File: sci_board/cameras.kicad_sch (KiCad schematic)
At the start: 4 parts, among them X1 TG2520SMN 24.0000M-MCGNNM0

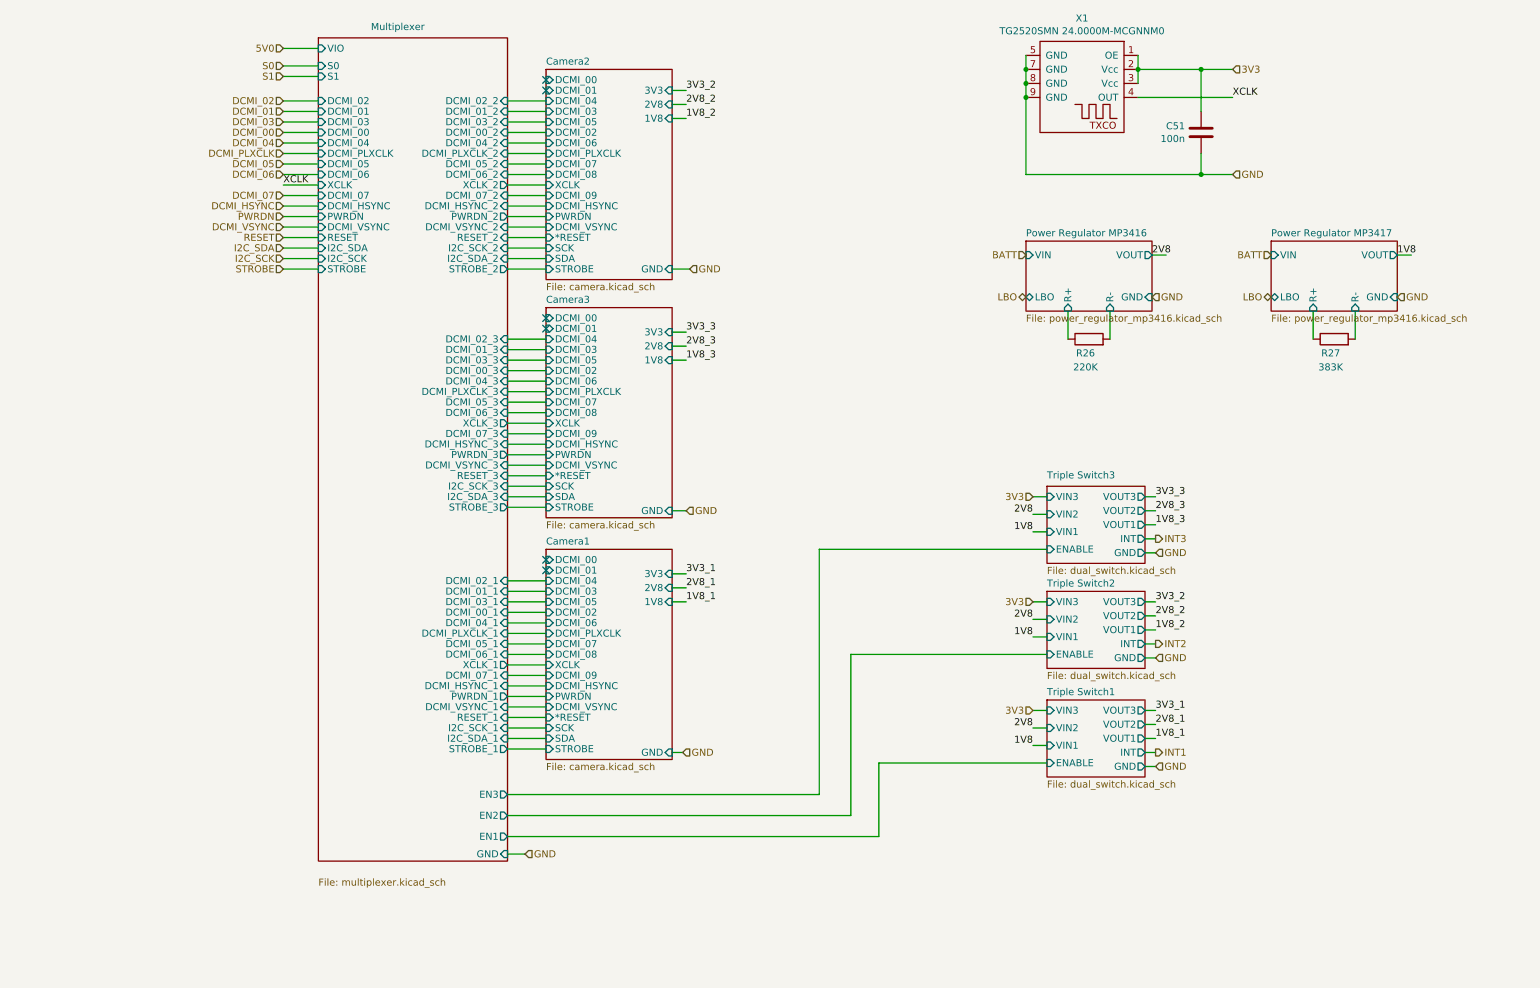
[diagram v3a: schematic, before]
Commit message: replace big multiplexers with tiny ones, replace boost converters with true ones
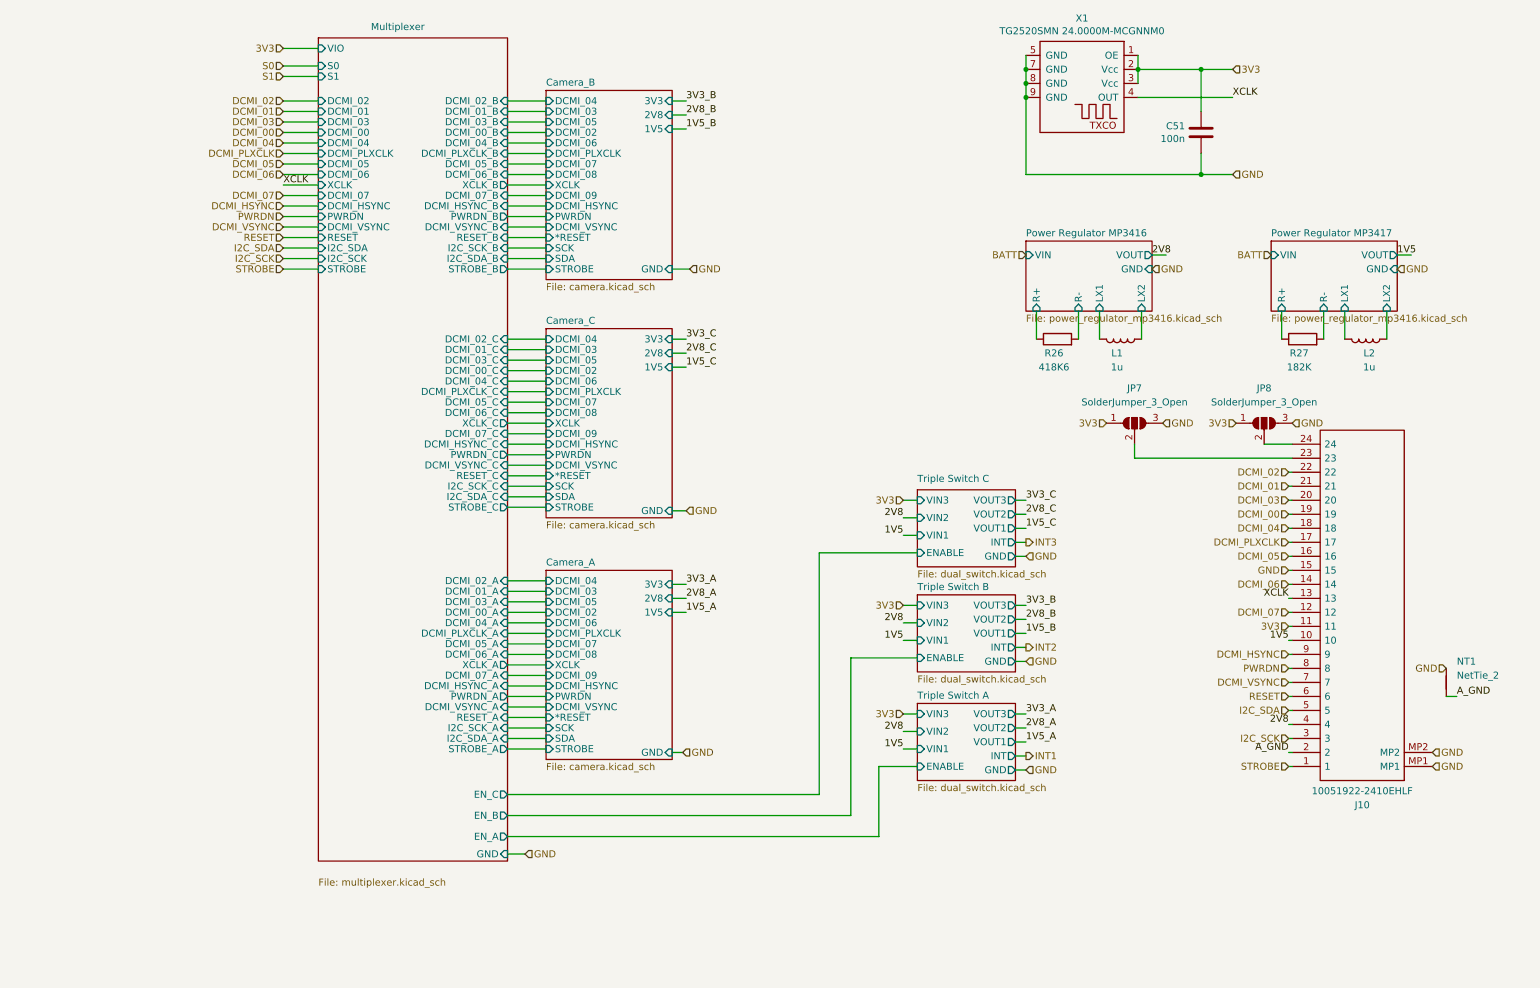
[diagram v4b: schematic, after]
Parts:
- added J10: 10051922-2410EHLF, Project:100519222410EHLF, symbol Project:10051922-2410EHLF
- added JP7, JP8: SolderJumper_3_Open, Jumper:SolderJumper-3_P2.0mm_Open_TrianglePad1.0x1.5mm, symbol Jumper:SolderJumper_3_Open
- added L1, L2: 1u, Inductor_SMD:L_1008_2520Metric_Pad1.43x2.20mm_HandSolder, symbol Device:L
- added NT1: NetTie_2, Project:NetTie-2_SMD_Pad0.3mm, symbol Device:NetTie_2
- R26: value 220K -> 418K6
- R27: value 383K -> 182K
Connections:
- net 2V8: now also J10.4
- net 3V3: now also J10.11, JP7.1 (A), JP8.1 (A)
- net DCMI_00: now also J10.19
- net DCMI_01: now also J10.21
- net DCMI_02: now also J10.22
- net DCMI_03: now also J10.20
- net DCMI_04: now also J10.18
- net DCMI_05: now also J10.16
- net DCMI_06: now also J10.14
- net DCMI_07: now also J10.12
- net DCMI_HSYNC: now also J10.9
- net DCMI_PLXCLK: now also J10.17
- net DCMI_VSYNC: now also J10.7
- net GND: now also J10.15, J10.MP1, J10.MP2, JP7.3 (B), JP8.3 (B), NT1.2
- net I2C_SCK: now also J10.3
- net I2C_SDA: now also J10.5
- net PWRDN: now also J10.8
- net RESET: now also J10.6
- net STROBE: now also J10.1
- net XCLK: now also J10.13
- new net: J10.24, JP8.2 (C)
- new net: J10.23, JP7.2 (C)
- new net 1V5: J10.10
- new net A_GND: J10.2, NT1.1
- new net Power Regulator MP3416/LX1: L1.2
- new net Power Regulator MP3416/LX2: L1.1
- new net Power Regulator MP3417/LX1: L2.2
- new net Power Regulator MP3417/LX2: L2.1
- no-connect marks 6 -> 0
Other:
- sheet Camera1 renamed Camera_A
- sheet Camera2 renamed Camera_B
- sheet Camera3 renamed Camera_C
- sheet Triple Switch1 renamed Triple Switch A
- sheet Triple Switch2 renamed Triple Switch B
- sheet Triple Switch3 renamed Triple Switch C
- sheet Camera_A ports: added 1V5; removed 1V8, DCMI_00, DCMI_01
- sheet Camera_B ports: added 1V5; removed 1V8, DCMI_00, DCMI_01
- sheet Camera_C ports: added 1V5; removed 1V8, DCMI_00, DCMI_01
- sheet Multiplexer ports: added DCMI_00_A, DCMI_00_B, DCMI_00_C, DCMI_01_A, DCMI_01_B, DCMI_01_C, DCMI_02_A, DCMI_02_B, DCMI_02_C, DCMI_03_A, DCMI_03_B, DCMI_03_C, DCMI_04_A, DCMI_04_B, DCMI_04_C, DCMI_05_A, DCMI_05_B, DCMI_05_C, DCMI_06_A, DCMI_06_B, DCMI_06_C, DCMI_07_A, DCMI_07_B, DCMI_07_C, DCMI_HSYNC_A, DCMI_HSYNC_B, DCMI_HSYNC_C, DCMI_PLXCLK_A, DCMI_PLXCLK_B, DCMI_PLXCLK_C, DCMI_VSYNC_A, DCMI_VSYNC_B, DCMI_VSYNC_C, EN_A, EN_B, EN_C, I2C_SCK_A, I2C_SCK_B, I2C_SCK_C, I2C_SDA_A, I2C_SDA_B, I2C_SDA_C, PWRDN_A, PWRDN_B, PWRDN_C, RESET_A, RESET_B, RESET_C, STROBE_A, STROBE_B, STROBE_C, XCLK_A, XCLK_B, XCLK_C; removed DCMI_00_1, DCMI_00_2, DCMI_00_3, DCMI_01_1, DCMI_01_2, DCMI_01_3, DCMI_02_1, DCMI_02_2, DCMI_02_3, DCMI_03_1, DCMI_03_2, DCMI_03_3, DCMI_04_1, DCMI_04_2, DCMI_04_3, DCMI_05_1, DCMI_05_2, DCMI_05_3, DCMI_06_1, DCMI_06_2, DCMI_06_3, DCMI_07_1, DCMI_07_2, DCMI_07_3, DCMI_HSYNC_1, DCMI_HSYNC_2, DCMI_HSYNC_3, DCMI_PLXCLK_1, DCMI_PLXCLK_2, DCMI_PLXCLK_3, DCMI_VSYNC_1, DCMI_VSYNC_2, DCMI_VSYNC_3, EN1, EN2, EN3, I2C_SCK_1, I2C_SCK_2, I2C_SCK_3, I2C_SDA_1, I2C_SDA_2, I2C_SDA_3, PWRDN_1, PWRDN_2, PWRDN_3, RESET_1, RESET_2, RESET_3, STROBE_1, STROBE_2, STROBE_3, XCLK_1, XCLK_2, XCLK_3
- sheet Power Regulator MP3416 ports: added LX1, LX2; removed LBO
- sheet Power Regulator MP3417 ports: added LX1, LX2; removed LBO
- moved on the sheet: R26, R27

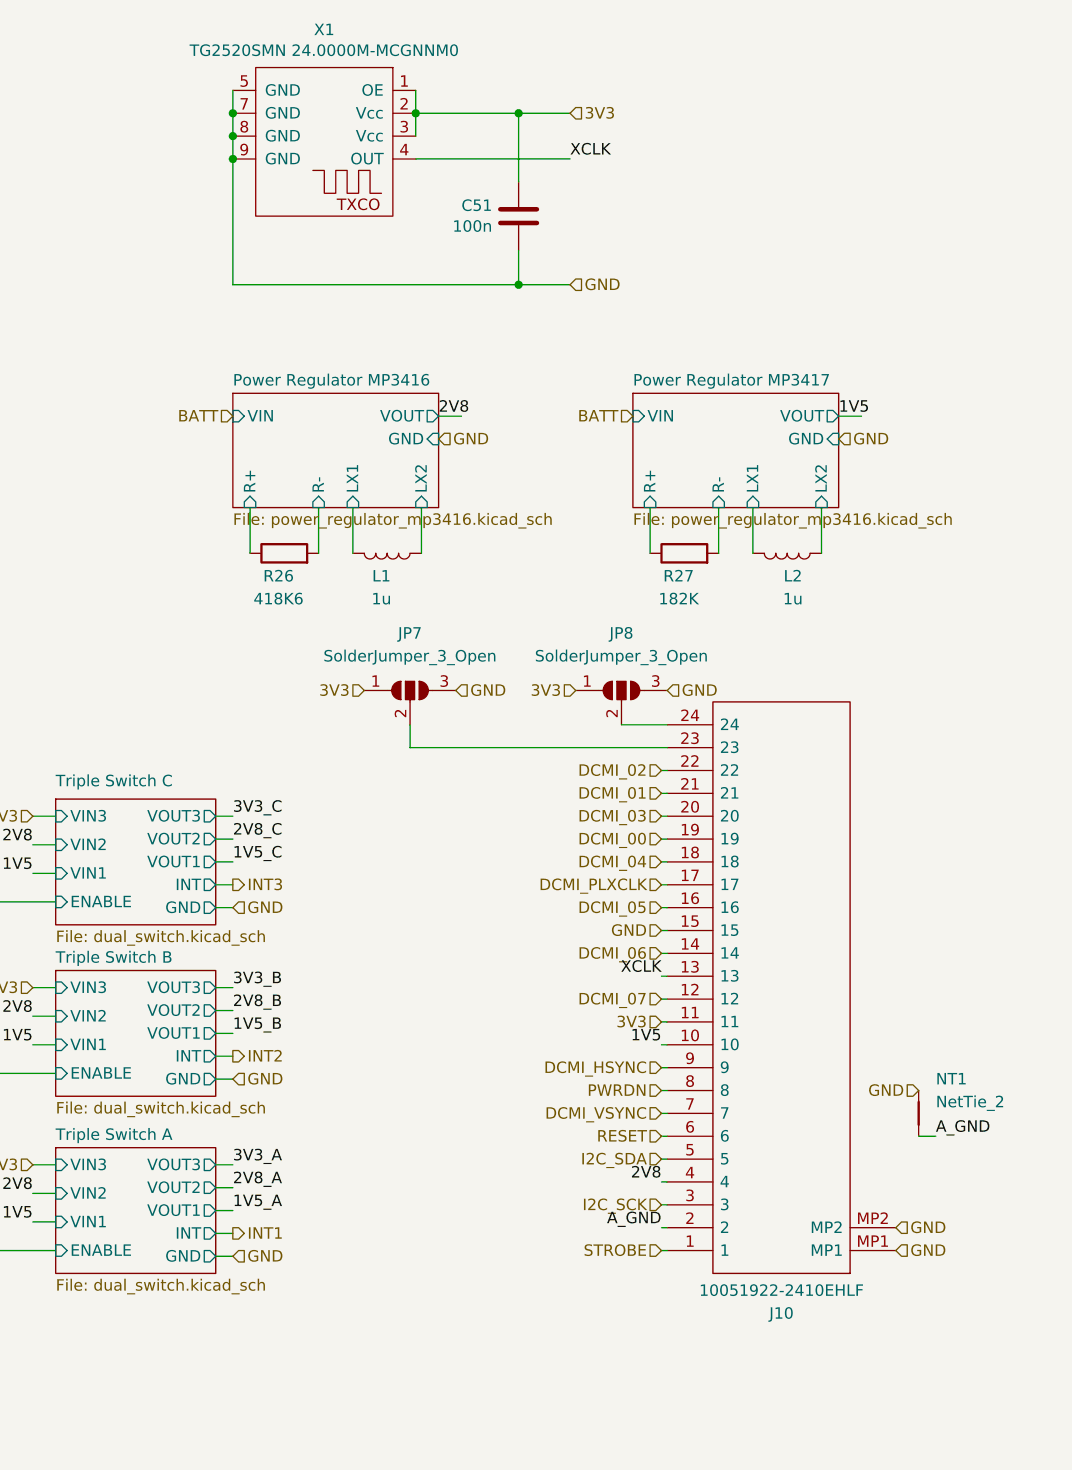
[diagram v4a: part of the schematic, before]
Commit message: changed over SCI to smaller footprint switches
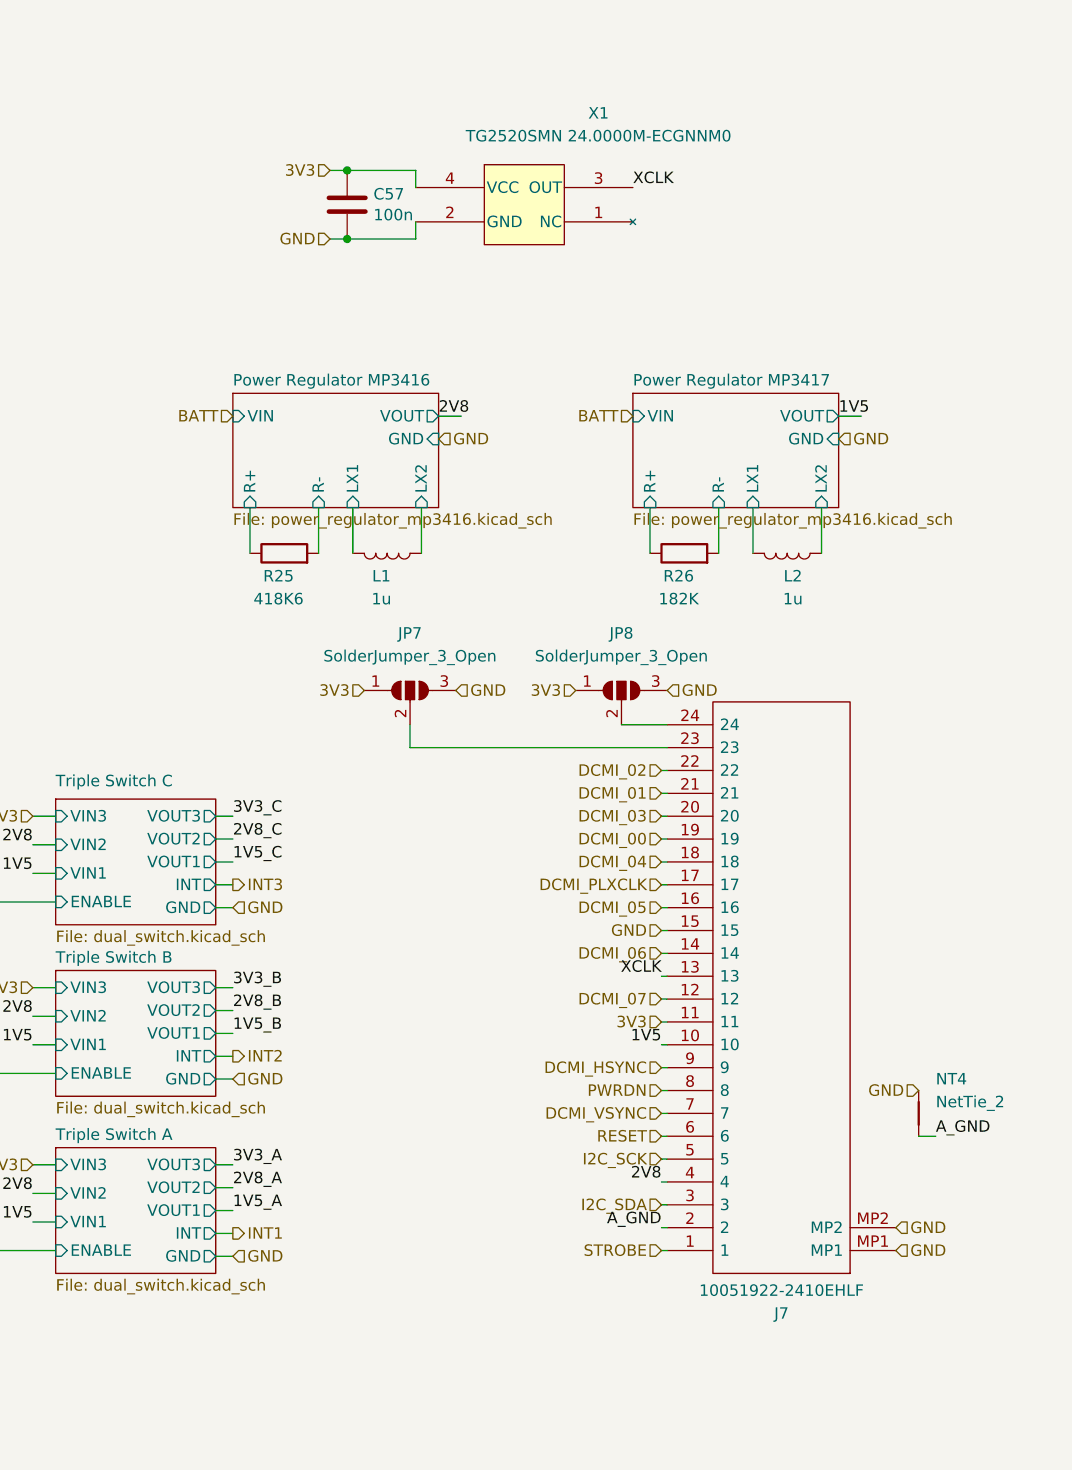
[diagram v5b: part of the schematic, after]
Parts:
- removed C51: 100n, Capacitor_SMD:C_0402_1005Metric_Pad0.74x0.62mm_HandSolder, symbol Device:C
- removed X1: TG2520SMN 24.0000M-MCGNNM0, Project:TG-3541CE_EPS, symbol Project:TG-3541CE-1K
- added C57: 100n, Capacitor_SMD:C_0402_1005Metric_Pad0.74x0.62mm_HandSolder, symbol Device:C
- added X1: TG2520SMN 24.0000M-ECGNNM0, Project:TG2520_EPS, symbol Project:TG2520SMN_EPS
- renumbered J10 to J7, NT1 to NT4, R26 to R25, R27 to R26
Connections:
- net 3V3: now also C57.1, X1.4 (VCC)
- net GND: now also C57.2, X1.2 (GND)
- net I2C_SCK: now also J7.5; no longer J7.3
- net I2C_SDA: now also J7.3; no longer J7.5
- net XCLK: now also X1.3 (OUT)

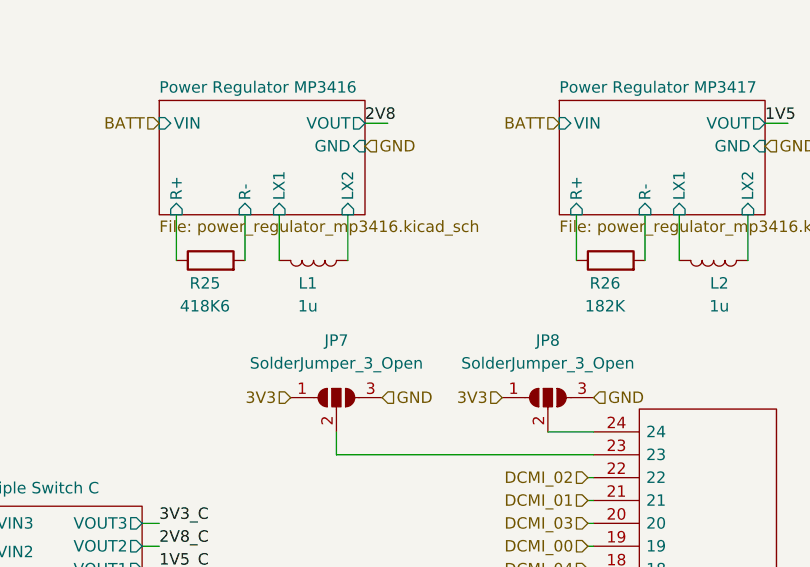
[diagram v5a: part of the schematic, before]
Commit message: replace nearly all buck converters with boost buck (missing is 5raw
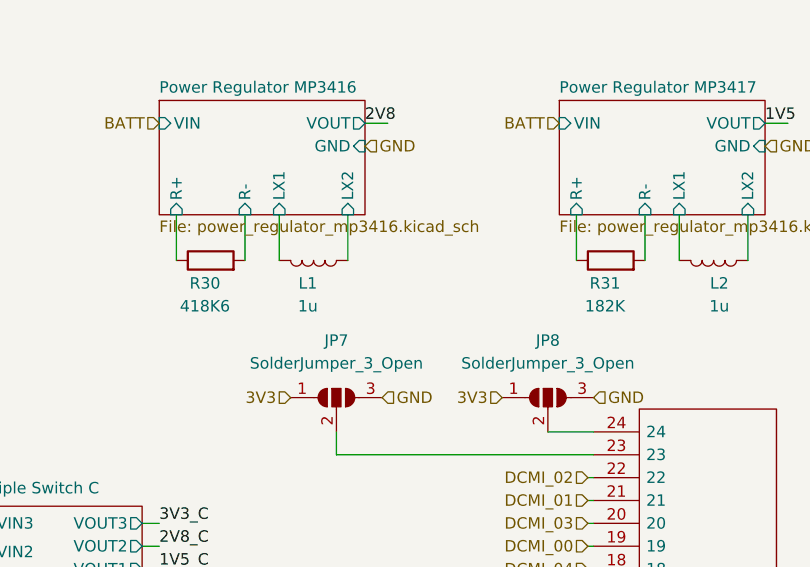
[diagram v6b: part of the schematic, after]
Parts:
- renumbered R25 to R30, R26 to R31
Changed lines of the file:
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@@
 		(on_board yes)
 		(dnp no)
-		(property "Reference" "R25"
+		(property "Reference" "R30"
 			(at 201.93 81.28 90)
 			(effects
@@
 			(project "sci_board"
 				(path "/b4b2c88d-f6cd-4e60-862d-e21f68728580/5e5b27f8-7a4c-45d0-95f8-aff71797fcd3"
-					(reference "R25")
+					(reference "R30")
 					(unit 1)
 				)
@@
 		(on_board yes)
 		(dnp no)
-		(property "Reference" "R26"
+		(property "Reference" "R31"
 			(at 246.38 81.28 90)
 			(effects
@@
 			(project "sci_board"
 				(path "/b4b2c88d-f6cd-4e60-862d-e21f68728580/5e5b27f8-7a4c-45d0-95f8-aff71797fcd3"
-					(reference "R26")
+					(reference "R31")
 					(unit 1)
 				)

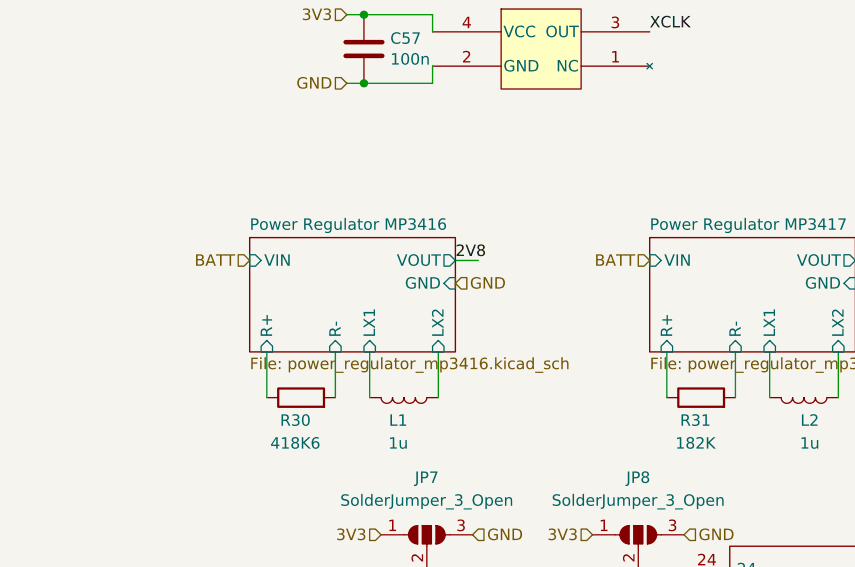
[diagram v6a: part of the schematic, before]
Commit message: SCI is based on PC104 connector
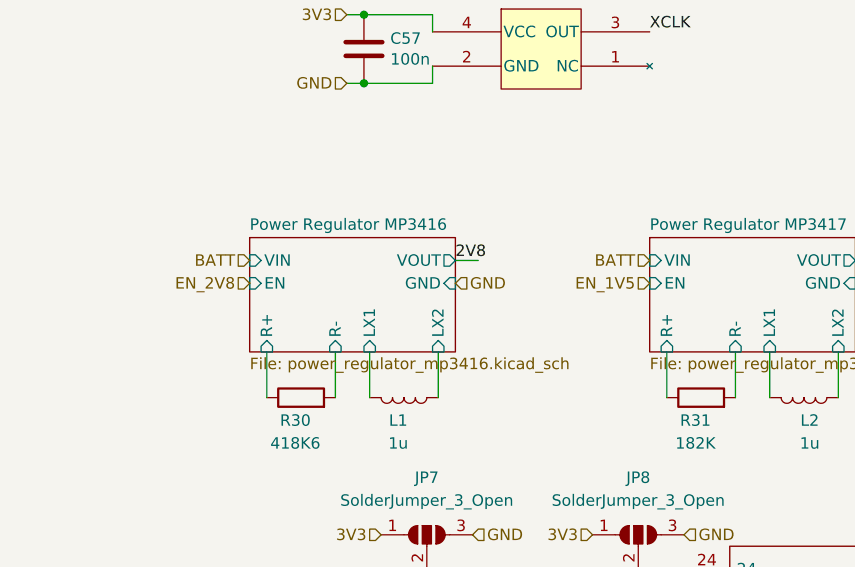
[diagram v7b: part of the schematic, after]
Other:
- sheet Power Regulator MP3416 ports: added EN; removed none
- sheet Power Regulator MP3417 ports: added EN; removed none
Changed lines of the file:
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@@
+		)
+	)
+	(hierarchical_label "EN_1V5"
+		(shape input)
+		(at 241.3 66.04 180)
+		(fields_autoplaced yes)
+		(effects
+			(font
+				(size 1.27 1.27)
+			)
+			(justify right)
 		)
 	)
@@
 		(shape input)
 		(at 244.475 120.65 180)
+		(fields_autoplaced yes)
+		(effects
+			(font
+				(size 1.27 1.27)
+			)
+			(justify right)
+		)
+	)
+	(hierarchical_label "EN_2V8"
+		(shape input)
+		(at 196.85 66.04 180)
 		(fields_autoplaced yes)
 		(effects
@@
 			)
 		)
+		(pin "EN" input
+			(at 241.3 66.04 180)
+			(effects
+				(font
+					(size 1.27 1.27)
+				)
+				(justify left)
+			)
+		)
 		(instances
 			(project "sci_board"
@@
 			(effects
 				(font
+					(size 1.27 1.27)
+				)
+				(justify left)
+			)
+		)
+		(pin "EN" input
+			(at 196.85 66.04 180)
+			(effects
+				(font
